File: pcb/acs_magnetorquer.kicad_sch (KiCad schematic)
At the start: 14 parts, among them J1 Conn_01x02, J2 Conn_01x02, U1 L293

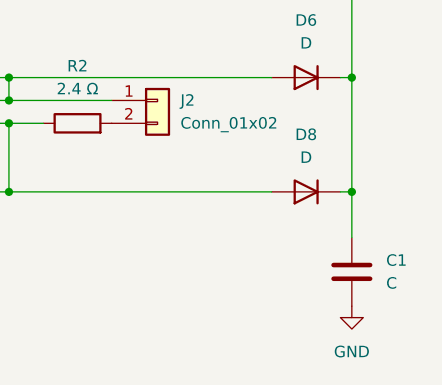
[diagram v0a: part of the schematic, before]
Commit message: fix: change mcu, add led
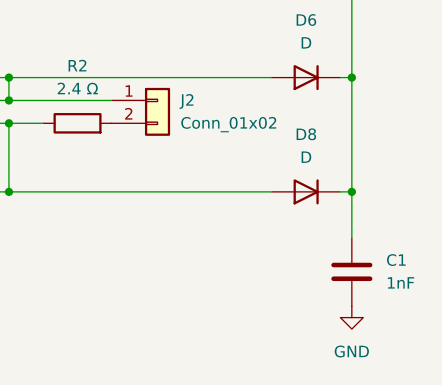
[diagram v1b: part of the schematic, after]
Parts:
- C1: value C -> 1nF; footprint Capacitor_THT:C_Radial_D4.0mm_H5.0mm_P1.50mm -> Capacitor_THT:C_Disc_D3.4mm_W2.1mm_P2.50mm
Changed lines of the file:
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@@
 			)
 		)
-		(property "Value" "C"
+		(property "Value" "1nF"
 			(at 187.96 102.8699 0)
 			(effects
@@
 			)
 		)
-		(property "Footprint" "Capacitor_THT:C_Radial_D4.0mm_H5.0mm_P1.50mm"
+		(property "Footprint" "Capacitor_THT:C_Disc_D3.4mm_W2.1mm_P2.50mm"
 			(at 185.1152 105.41 0)
 			(effects
